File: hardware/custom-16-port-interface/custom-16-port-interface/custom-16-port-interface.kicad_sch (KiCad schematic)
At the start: 0 parts

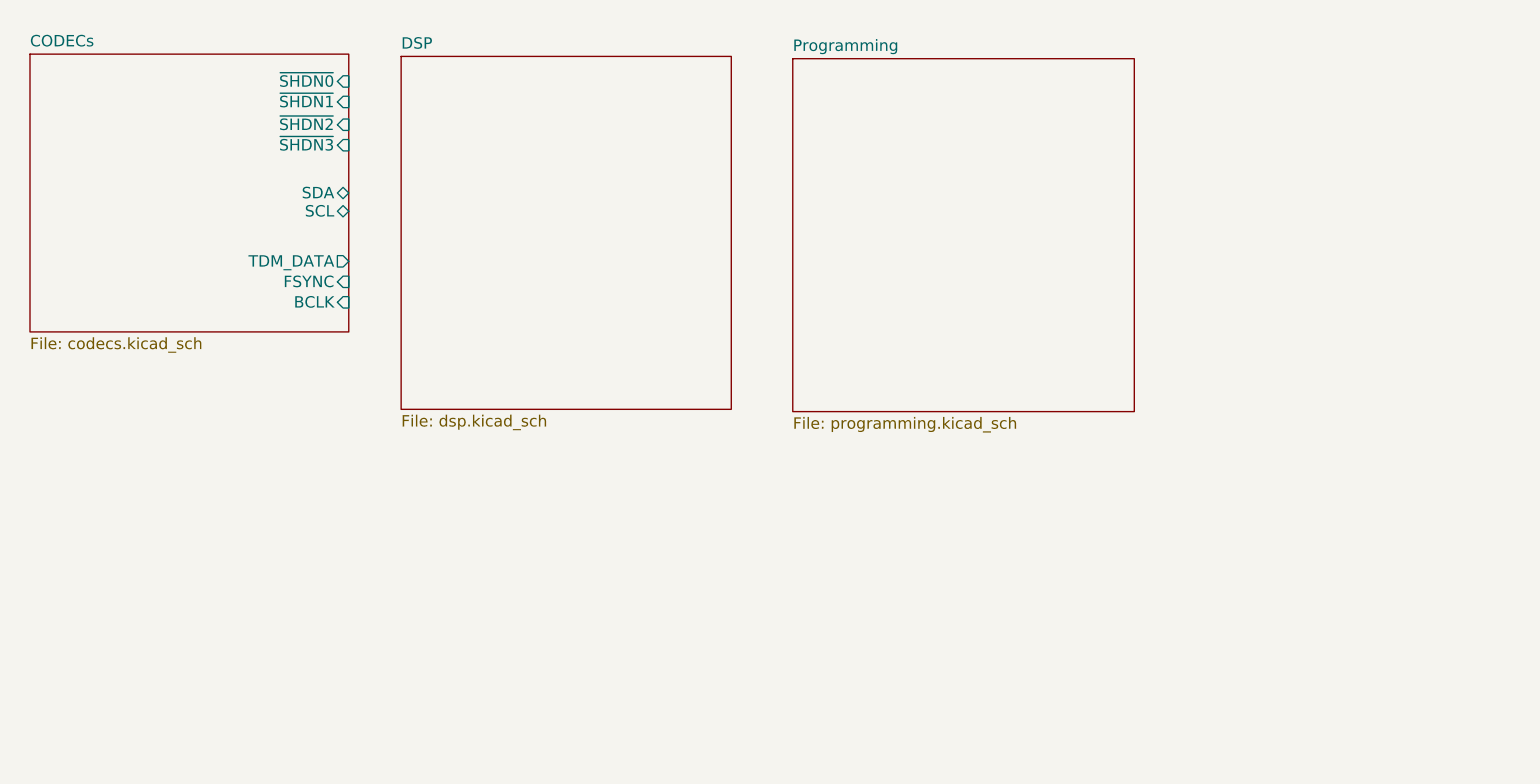
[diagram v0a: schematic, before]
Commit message: Added fpga firmware for ADAT->TDM, updated schematic
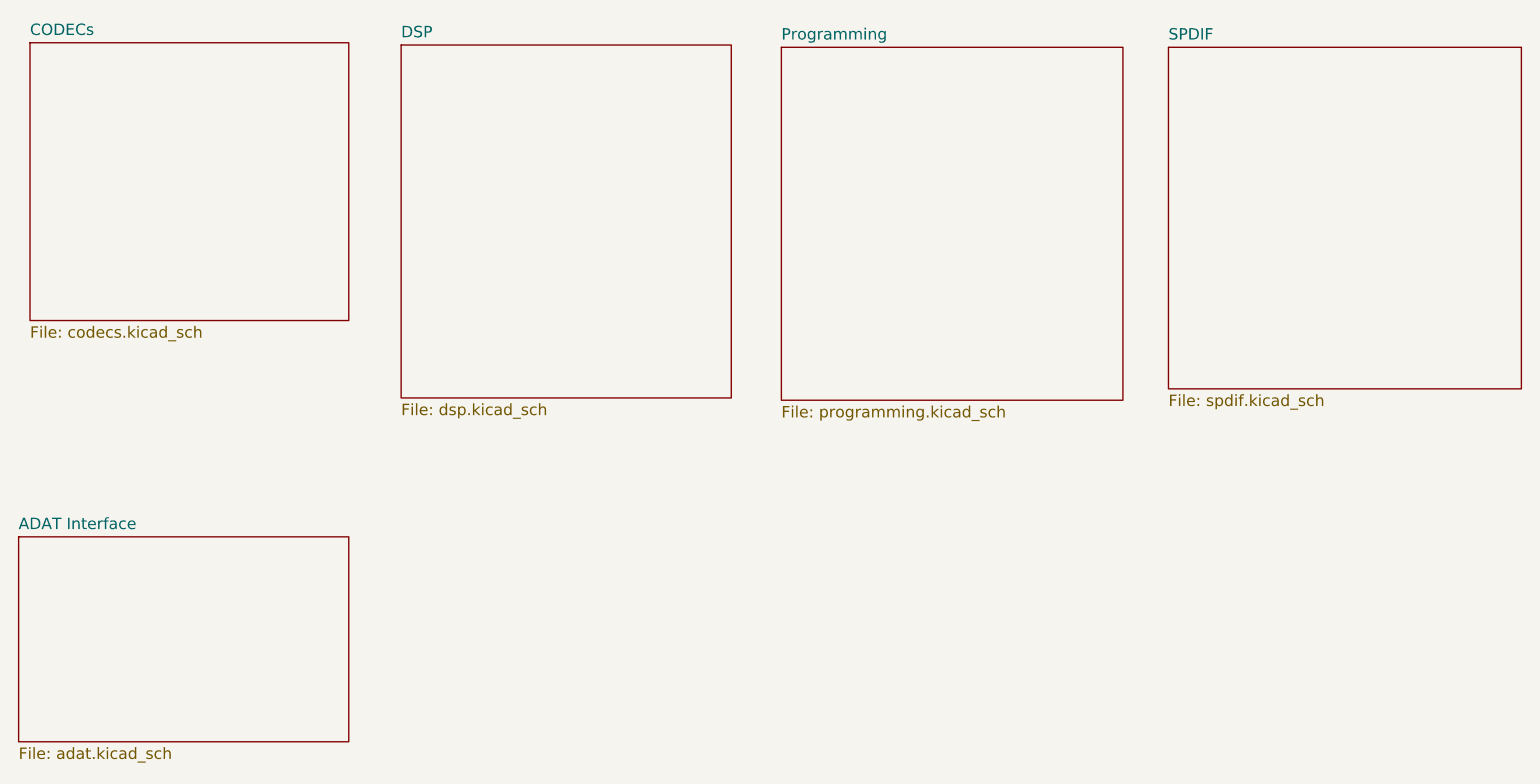
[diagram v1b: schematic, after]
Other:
- added sheet ADAT Interface (adat.kicad_sch)
- added sheet SPDIF (spdif.kicad_sch)
- sheet CODECs ports: added none; removed BCLK, FSYNC, SCL, SDA, TDM_DATA, ~{SHDN0}, ~{SHDN1}, ~{SHDN2}, ~{SHDN3}
